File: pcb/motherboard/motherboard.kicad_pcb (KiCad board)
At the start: 2 copper layers, 35 parts, among them J1 UART, U1 Huzzah32

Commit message: Pin orientation
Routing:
- net (no net): track 169.5 -> 0.00 mm
- net GND: track 344.3 -> 381.1 mm
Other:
- board outline added: 160 x 96.5 mm

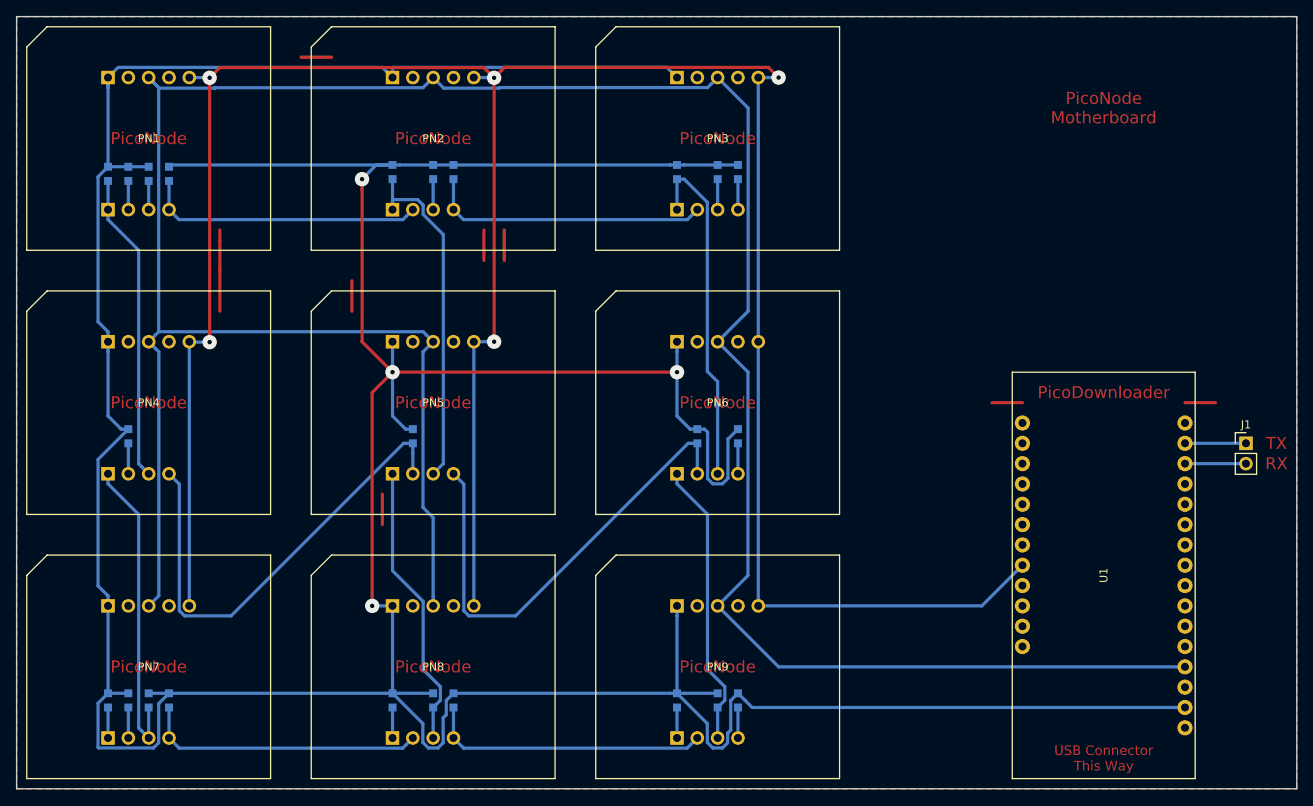
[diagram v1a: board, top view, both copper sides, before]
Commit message: Bring our own voltage regulator instead of using the Huzzah32's built-in
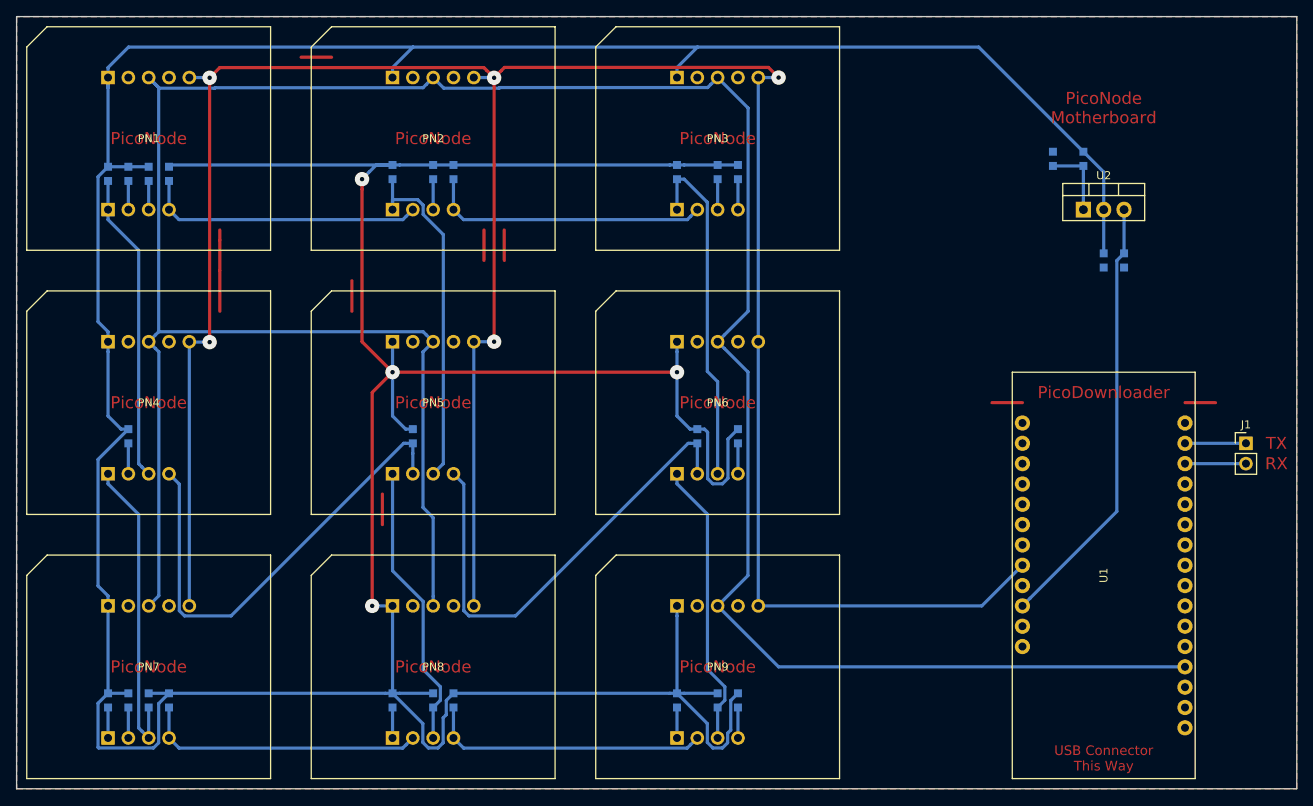
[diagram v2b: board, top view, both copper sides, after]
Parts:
- added C1: 0.1µF, Capacitor_SMD:C_0603_1608Metric_Pad0.99x1.00mm_HandSolder, B.Cu at (188.0, 63.5)
- added C2: 1.0µF, Capacitor_SMD:C_0603_1608Metric_Pad0.99x1.00mm_HandSolder, B.Cu at (185.4, 63.5)
- added R15: 240, Resistor_SMD:R_0603_1608Metric_Pad0.99x1.00mm_HandSolder, B.Cu at (182.9, 50.8)
- added R16: 390, Resistor_SMD:R_0603_1608Metric_Pad0.99x1.00mm_HandSolder, B.Cu at (179.1, 50.8)
- added U2: LM317_3PinPackage, Package_TO_SOT_THT:TO-220-3_Vertical, F.Cu at (182.9, 57.1)
- renumbered R15 to R17, R16 to R18, R17 to R19, R18 to R20, R19 to R21, R20 to R22, R21 to R23, R22 to R24, R23 to R25, R24 to R26
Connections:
- U1 pad 14: VDD -> Net-(U1-Pad14)
- U1 pad 3: (no net) -> VBUS
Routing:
- net VBUS: track 0.00 -> 54.8 mm
- net VDD: track 581.6 -> 604.1 mm
- net Net-(R15-Pad2): track 0.00 -> 9.27 mm

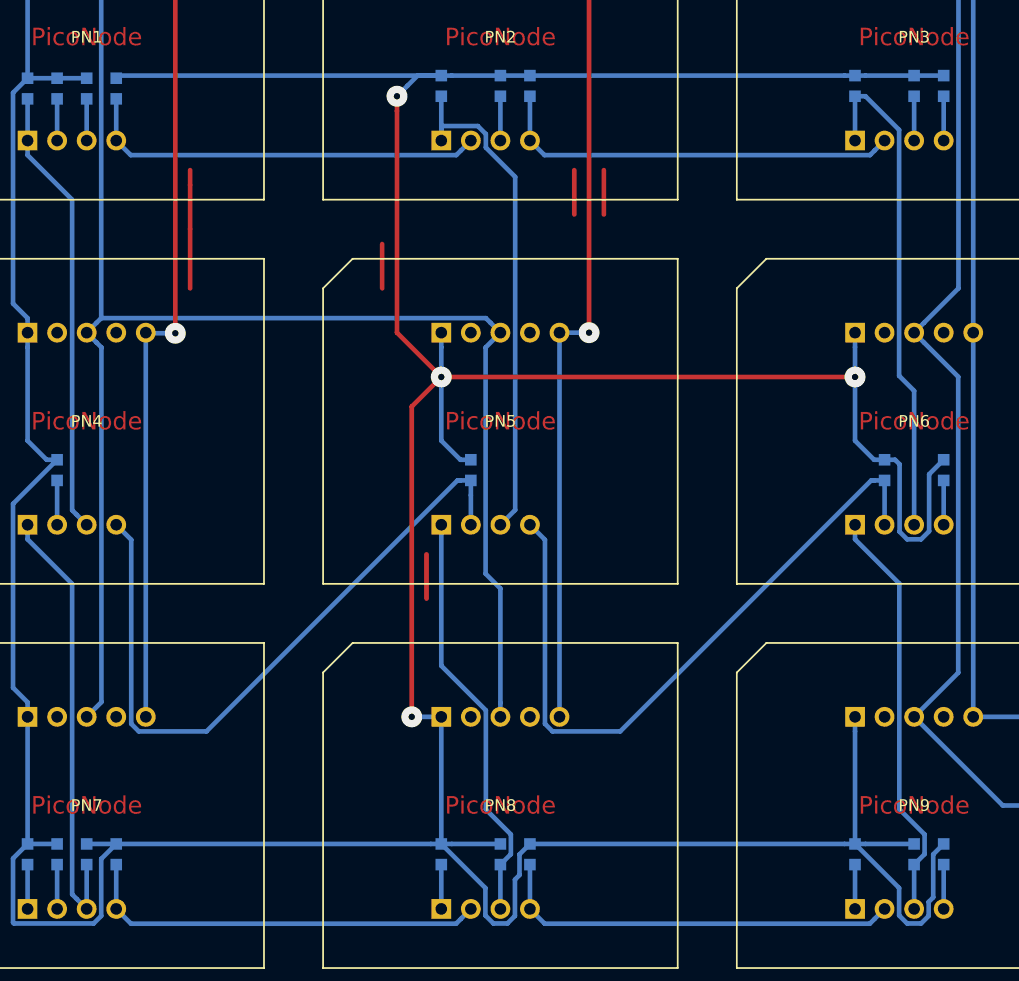
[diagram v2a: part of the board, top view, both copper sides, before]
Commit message: Via optimization
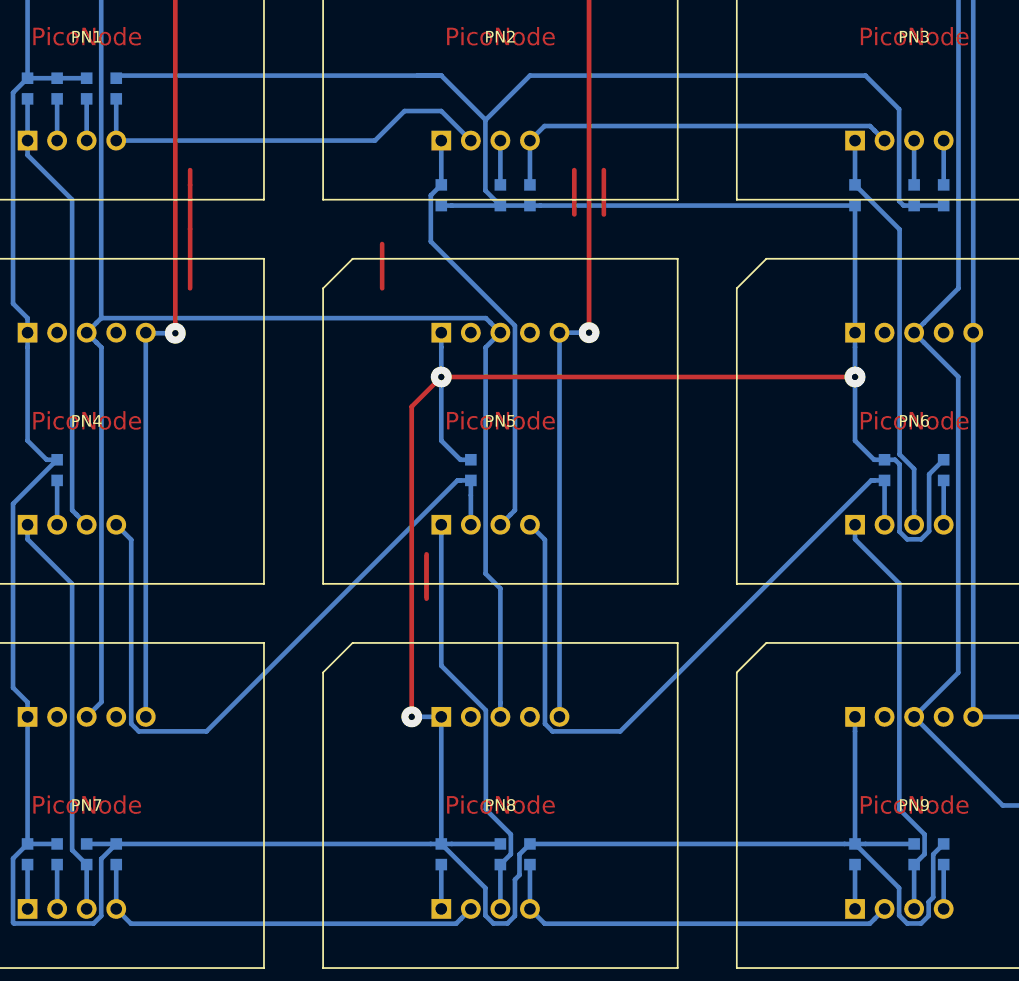
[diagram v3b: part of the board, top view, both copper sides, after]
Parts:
- moved R10 9.39 mm to (139.7, 61.8), turned to 90 degrees
- moved R5 9.39 mm to (96.5, 61.8), turned to 90 degrees
- moved R6 9.39 mm to (101.6, 61.8), turned to 90 degrees
- moved R7 9.39 mm to (104.1, 61.8), turned to 90 degrees
- moved R8 9.39 mm to (132.1, 61.8), turned to 90 degrees
- moved R9 9.39 mm to (137.2, 61.8), turned to 90 degrees
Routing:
- net VDD: track 604.1 -> 642.7 mm, vias 4 -> 3
- net Net-(PN3-Pad6): track 43.3 -> 35.1 mm
- net Net-(PN2-Pad6): track 44.3 -> 36.9 mm
- net Net-(PN4-Pad6): track 38.9 -> 35.1 mm
- net Net-(PN1-Pad9): track 35.1 -> 36.2 mm
